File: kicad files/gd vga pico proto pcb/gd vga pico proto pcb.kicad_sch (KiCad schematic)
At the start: 0 parts

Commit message: floor planning complete
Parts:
- added C1: 10u, Capacitor_SMD:C_0805_2012Metric, symbol My Library:C_0805
- added C2, C3, C4: 1u, Capacitor_SMD:C_0805_2012Metric, symbol My Library:C_0805
- added J1: RGB Bin, Connector_PinSocket_2.54mm:PinSocket_2x04_P2.54mm_Vertical, symbol Connector_Generic:Conn_02x04_Odd_Even
- added J2: CLKS, Connector_PinSocket_2.54mm:PinSocket_2x04_P2.54mm_Vertical, symbol Connector_Generic:Conn_02x04_Odd_Even
- added J3: Conn_01x05, Connector_PinHeader_2.54mm:PinHeader_1x05_P2.54mm_Vertical, symbol Connector_Generic:Conn_01x05
- added J4: L77HDE15SD1CH4F, Connector_Dsub:DSUB-15-HD_Female_Horizontal_P2.29x1.98mm_EdgePinOffset8.35mm_Housed_MountingHolesOffset10.89mm, symbol Connector:DB15_Female_HighDensity_MountingHoles
- added J5: VID_TXRX, Connector_PinHeader_2.54mm:PinHeader_1x04_P2.54mm_Vertical, symbol Connector_Generic:Conn_01x04
- added J6: WIN, Connector_PinHeader_2.54mm:PinHeader_1x02_P2.54mm_Vertical, symbol Connector_Generic:Conn_01x02
- added J7: 5V, Connector_PinSocket_2.54mm:PinSocket_1x04_P2.54mm_Vertical, symbol Connector_Generic:Conn_01x04
- added JP1: 14M, Jumper:SolderJumper-2_P1.3mm_Bridged_RoundedPad1.0x1.5mm, symbol Jumper:SolderJumper_2_Bridged
- added JP2: 7M, Jumper:SolderJumper-2_P1.3mm_Open_TrianglePad1.0x1.5mm, symbol Jumper:SolderJumper_2_Open
- added R1, R10, R11: 100, Resistor_SMD:R_0603_1608Metric, symbol My_Library:R_0805
- added R2, R5, R8: 1k, Resistor_SMD:R_0603_1608Metric, symbol Device:R
- added R3: 390, Resistor_SMD:R_0603_1608Metric, symbol Device:R
- added R4, R7: 2k2, Resistor_SMD:R_0603_1608Metric, symbol Device:R
- added R6, R9: 470, Resistor_SMD:R_0603_1608Metric, symbol Device:R
- added RNP1, RNP2: 4k7, Resistor_SMD:R_0603_1608Metric, symbol My_Library:R_0805
- added SW1: RESET, My Libraries:SW_Push_CK_PTS525_SM15, symbol Switch:SW_Push
- added TP1, TP2, TP3, TP4, TP5, TP6, TP7, TP8: TestPoint_Harwin, My Libraries:Harwin-S1751-46-Test-Point, symbol My Library:TestPoint_Harwin
- added U1: Pico, RPi_Pico:RPi_Pico_SMD_TH, symbol RPi_Pico:Pico
- added U2: 74HCT245, Package_SO:SO-20_5.3x12.6mm_P1.27mm, symbol 74xx:74HC245
- added U3, U4: 74LVC2G04, Package_TO_SOT_SMD:SOT-23-6, symbol 74xGxx:74LVC2G04
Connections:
- new net: U3.3, U3.6
- new net: J4.13, R10.1
- new net: J4.14, R11.1
- new net: J4.9, R1.2
- new net: U4.3, U4.6
- new net +3.3V: U3.5 (+3.3V), U3.5 (+3.3V), U4.5 (+3.3V), U4.5 (+3.3V)
- new net +3V3: C2.1, C3.1, C4.1, J3.1 (Pin_1), RNP1.2, RNP2.2, U1.36 (3V3), U2.20 (VCC)
- new net +5V: C1.1, J7.1 (Pin_1), J7.2 (Pin_2), R1.1, U1.39 (VSYS), U2.1 (A->B)
- new net 14M: J2.1 (Pin_1), JP1.1 (A)
- new net 14M_J: JP1.2 (B), U2.9 (A7)
- new net 14M_RP: U1.22 (GPIO17), U2.12 (B6)
- new net 7M: J2.2 (Pin_2), JP2.1 (A)
- new net 7M_J: JP2.2 (B), U2.8 (A6)
- new net 7M_RP: U1.21 (GPIO16), U2.11 (B7)
- new net BLU0: R7.2, U1.7 (GPIO5)
- new net BLU1: R8.2, U1.9 (GPIO6)
- new net BLU2: R9.2, U1.10 (GPIO7)
- new net CREF: J2.3 (Pin_3)
- new net GND: C1.2, C2.2, C3.2, C4.2, J1.7 (Pin_7), J1.8 (Pin_8), J2.7 (Pin_7), J2.8 (Pin_8), J3.5 (Pin_5), J4.0, J4.10, J4.5, J4.6, J4.7, J4.8, J5.4 (Pin_4), J6.2 (Pin_2), J7.3 (Pin_3), J7.4 (Pin_4), SW1.2, TP4.1, TP5.1, U1.13 (GND), U1.18 (GND), U1.23 (GND), U1.28 (GND), U1.3 (GND), U1.33 (AGND), U1.38 (GND), U1.42 (GND), U1.8 (GND), U2.10 (GND), U2.19 (CE), U3.2 (GND), U3.2 (GND), U4.2 (GND), U4.2 (GND)
- new net GPIO10: U1.14 (GPIO10)
- new net GRN0: R4.2, U1.4 (GPIO2)
- new net GRN1: R5.2, U1.5 (GPIO3)
- new net GRN2: R6.2, U1.6 (GPIO4)
- new net HSYNC: R10.2, TP2.1, U1.11 (GPIO8)
- new net PH0: J2.5 (Pin_5)
- new net PICO_EN: TP1.1
- new net Q3: J2.4 (Pin_4)
- new net RED0: R2.2, U1.1 (GPIO0)
- new net RED1: R3.2, U1.2 (GPIO1)
- new net RGB1: J1.3 (Pin_3), U2.5 (A3)
- new net RGB1_RP: U1.24 (GPIO18), U2.15 (B3)
- new net RGB2: J1.5 (Pin_5), U2.4 (A2)
- new net RGB2_RP: U1.25 (GPIO19), U2.16 (B2)
- new net RGB4: J1.2 (Pin_2), U2.3 (A1)
- new net RGB4_RP: U1.26 (GPIO20), U2.17 (B1)
- new net RGB8: J1.4 (Pin_4), U2.2 (A0)
- new net RGB8_RP: U1.27 (GPIO21), U2.18 (B0)
- new net RUN: J3.4 (Pin_4), SW1.1, U1.30 (RUN)
- new net SERVIDEO: J1.6 (Pin_6), U3.1
- new net SERVID_RP: U1.29 (GPIO22), U3.4
- new net SWCLK: J3.3 (Pin_3), U1.41 (SWCLK)
- new net SWDIO: J3.2 (Pin_2), U1.43 (SWDIO)
- new net VBUS: U1.40 (VBUS)
- new net VGA_B: J4.3, R7.1, R8.1, R9.1, TP8.1
- new net VGA_G: J4.2, R4.1, R5.1, R6.1, TP7.1
- new net VGA_R: J4.1, R2.1, R3.1, TP6.1
- new net VGA_SCL: J4.15, RNP2.1, U1.32 (GPIO27_ADC1)
- new net VGA_SDA: J4.12, RNP1.1, U1.31 (GPIO26_ADC0)
- new net VID_RX: J5.3 (Pin_3), U1.17 (GPIO13)
- new net VID_TX: J5.2 (Pin_2), U1.16 (GPIO12)
- new net VIN_EN: J5.1 (Pin_1), U1.15 (GPIO11)
- new net VSYNC: R11.2, TP3.1, U1.12 (GPIO9)
- new net ~{RESET_RP}: U1.34 (GPIO28_ADC2), U4.4
- new net ~{RESET}: J2.6 (Pin_6), U4.1
- new net ~{SYNC_RP}: U1.19 (GPIO14), U2.14 (B4)
- new net ~{SYNC}: J1.1 (Pin_1), U2.6 (A4)
- new net ~{WINDOW_RP}: U1.20 (GPIO15), U2.13 (B5)
- new net ~{WINDOW}: J6.1 (Pin_1), U2.7 (A5)
- no-connect marks 0 -> 3
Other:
- note added: "Pico"
- note added: "VGA"
- note added: "VGA 'DAC'"

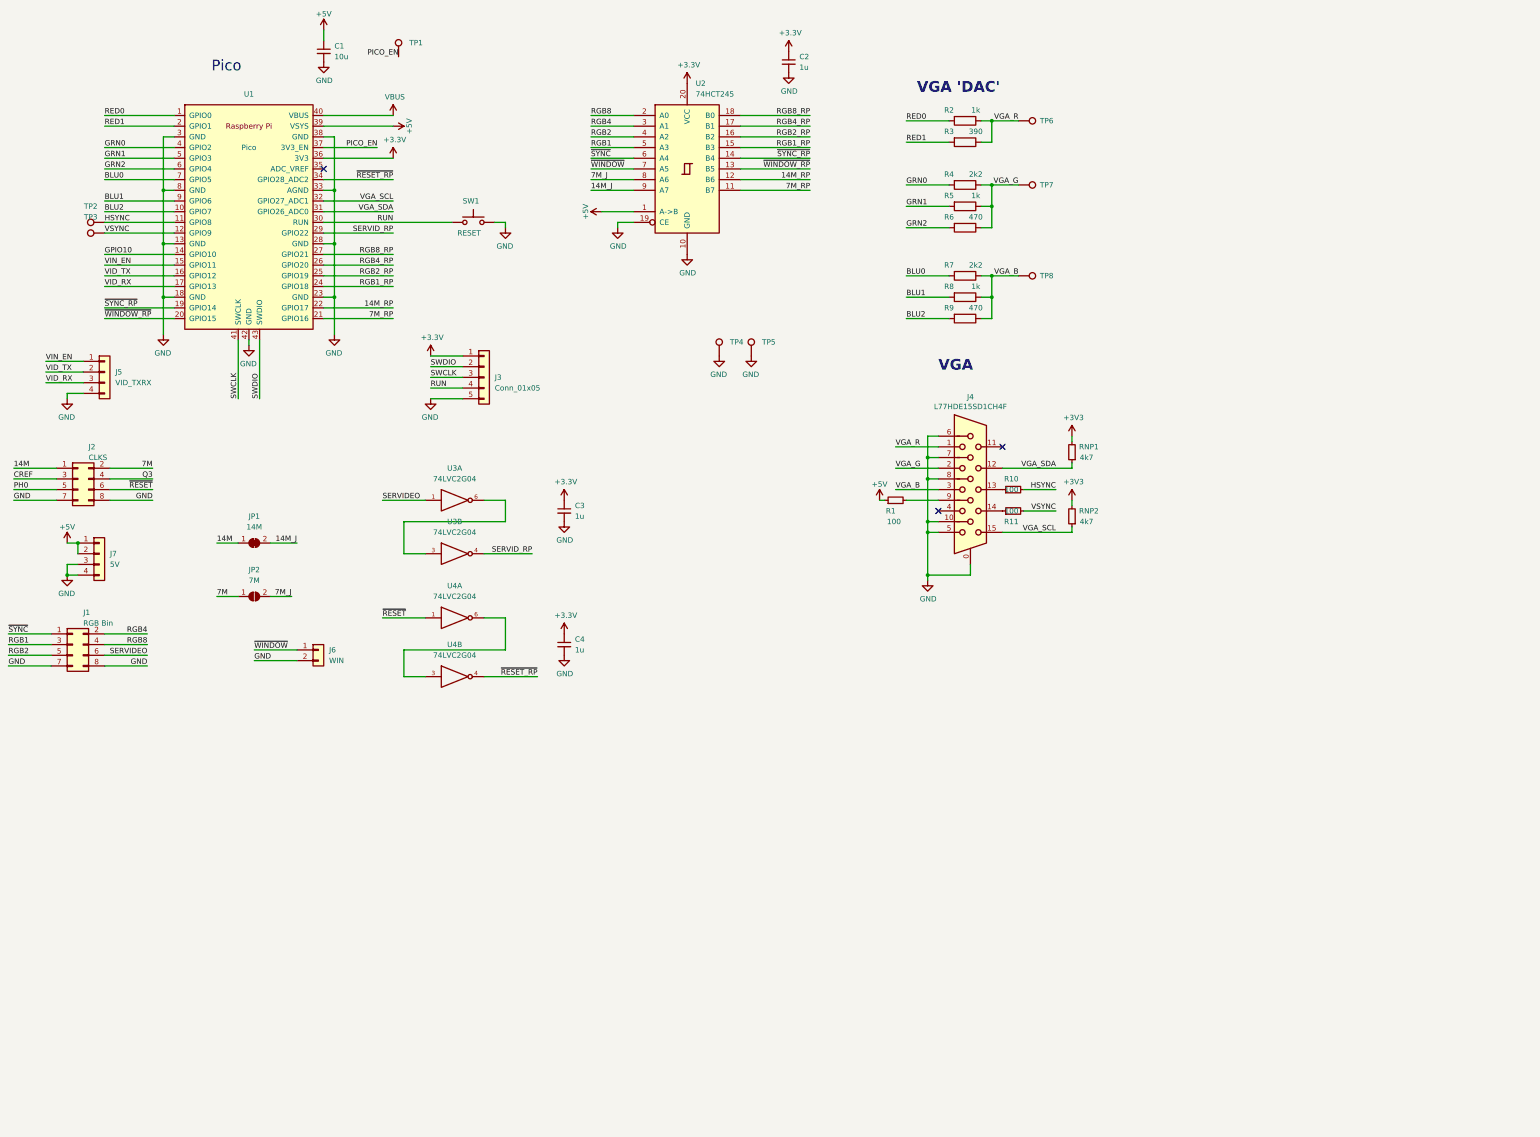
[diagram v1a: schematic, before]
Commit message: swapped from pico to RP2040--yay
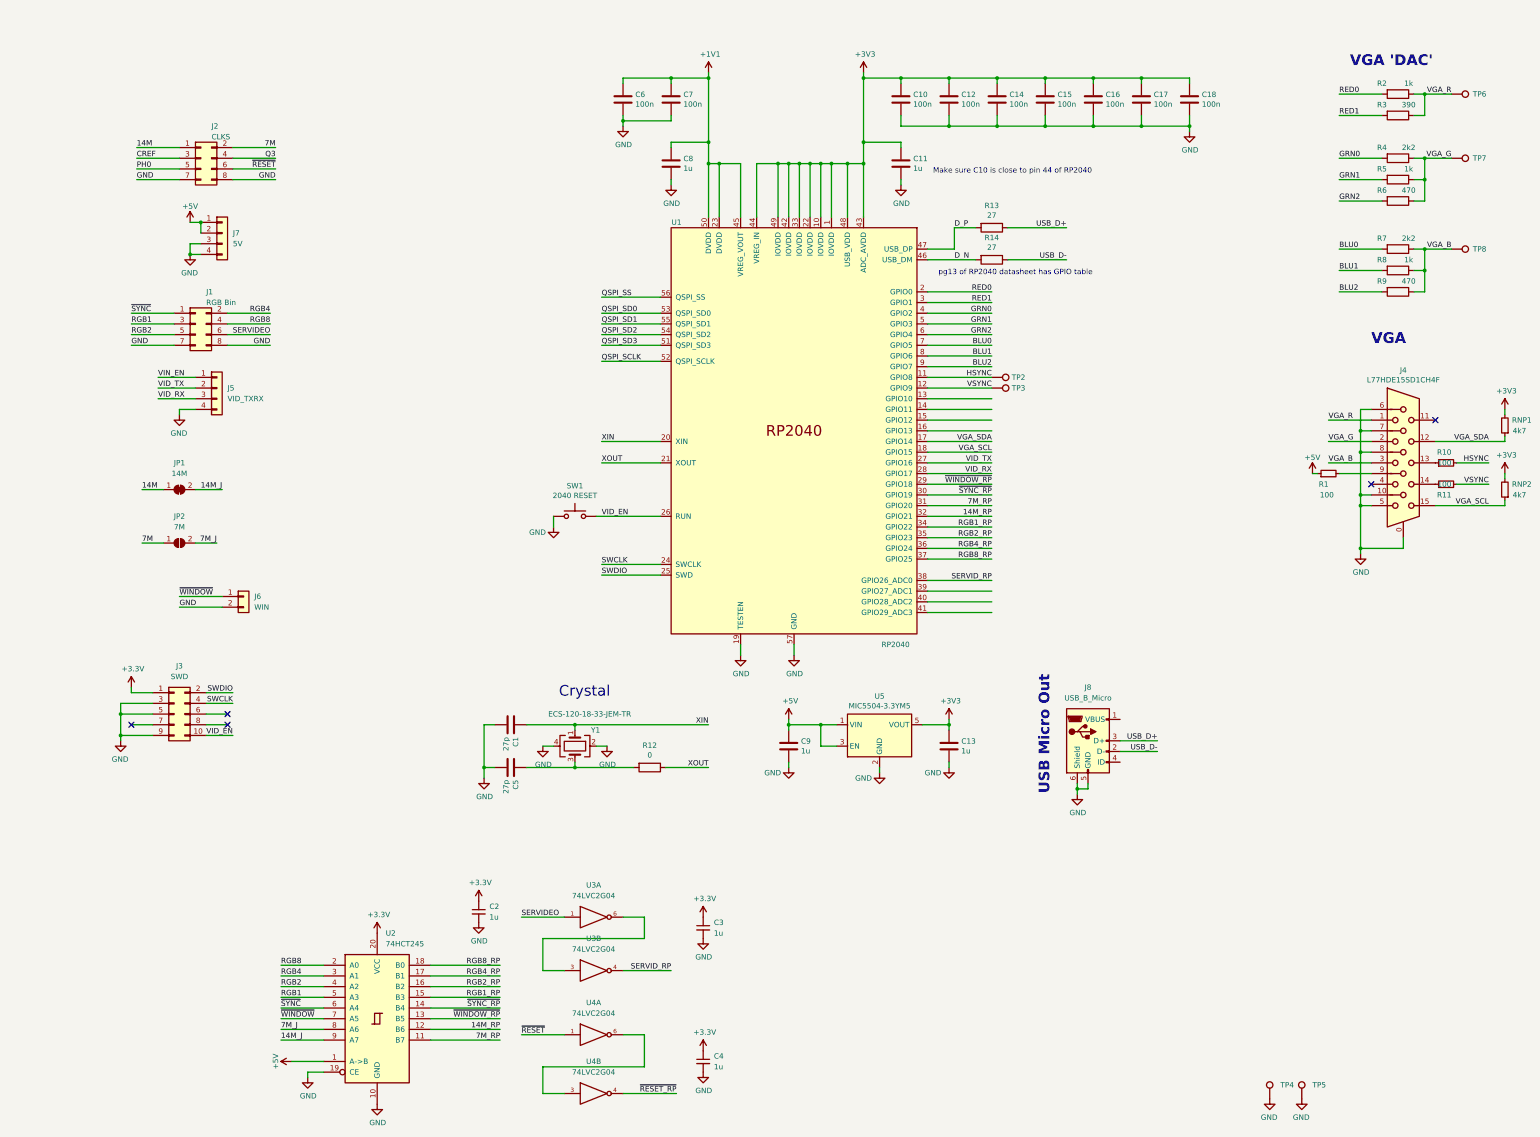
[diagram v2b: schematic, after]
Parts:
- removed C1: 10u, Capacitor_SMD:C_0805_2012Metric, symbol My Library:C_0805
- removed J3: Conn_01x05, Connector_PinHeader_2.54mm:PinHeader_1x05_P2.54mm_Vertical, symbol Connector_Generic:Conn_01x05
- removed TP1: TestPoint_Harwin, My Libraries:Harwin-S1751-46-Test-Point, symbol My Library:TestPoint_Harwin
- removed U1: Pico, RPi_Pico:RPi_Pico_SMD_TH, symbol RPi_Pico:Pico
- added C1, C5: 27p, Capacitor_SMD:C_0603_1608Metric, symbol Device:C
- added C10, C12, C14, C15, C16, C17, C18, C6, C7: 100n, Capacitor_SMD:C_0603_1608Metric, symbol Device:C
- added C11, C8: 1u, Capacitor_SMD:C_0603_1608Metric, symbol Device:C
- added C13, C9: 1u, Capacitor_SMD:C_0805_2012Metric, symbol Device:C
- added J3: SWD, Connector_PinSocket_1.27mm:PinSocket_2x05_P1.27mm_Vertical_SMD, symbol Connector_Generic:Conn_02x05_Odd_Even
- added J8: USB_B_Micro, Connector_USB:USB_Micro-B_GCT_USB3076-30-A, symbol Connector:USB_B_Micro
- added R12: 0, Resistor_SMD:R_0603_1608Metric, symbol Device:R
- added R13, R14: 27, Resistor_SMD:R_0603_1608Metric, symbol Device:R
- added U1: RP2040, RP2040_minimal:RP2040-QFN-56, symbol MCU_RaspberryPi_RP2040:RP2040
- added U5: MIC5504-3.3YM5, Package_TO_SOT_SMD:SOT-23-5, symbol Regulator_Linear:MIC5504-3.3YM5
- added Y1: ECS-120-18-33-JEM-TR, Crystal:Crystal_SMD_3225-4Pin_3.2x2.5mm, symbol Device:Crystal_GND24
- SW1: value RESET -> 2040 RESET
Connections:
- net RUN is gone; now on net GND: SW1.1
- net +3V3: now also C10.1, C11.1, C12.1, C13.1, C14.1, C15.1, C16.1, C17.1, C18.1, J3.1 (Pin_1), U1.1 (IOVDD), U1.10 (IOVDD), U1.22 (IOVDD), U1.33 (IOVDD), U1.42 (IOVDD), U1.43 (ADC_AVDD), U1.44 (VREG_IN), U1.48 (USB_VDD), U1.49 (IOVDD), U5.5 (VOUT)
- net +5V: now also C9.1, U5.1 (VIN), U5.3 (EN)
- net 14M_RP: now also U1.32 (GPIO21)
- net 7M_RP: now also U1.31 (GPIO20)
- net BLU0: now also U1.7 (GPIO5)
- net BLU1: now also U1.8 (GPIO6)
- net BLU2: now also U1.9 (GPIO7)
- net GND: now also C1.2, C10.2, C11.2, C12.2, C13.2, C14.2, C15.2, C16.2, C17.2, C18.2, C5.2, C6.2, C7.2, C8.2, C9.2, J3.3 (Pin_3), J3.5 (Pin_5), J3.9 (Pin_9), J8.5 (GND), J8.6 (Shield), U1.19 (TESTEN), U1.57 (GND), U5.2 (GND), Y1.2, Y1.4; no longer SW1.2
- net GRN0: now also U1.4 (GPIO2)
- net GRN1: now also U1.5 (GPIO3)
- net GRN2: now also U1.6 (GPIO4)
- net HSYNC: now also U1.11 (GPIO8)
- net RED0: now also U1.2 (GPIO0)
- net RED1: now also U1.3 (GPIO1)
- net RGB1_RP: now also U1.34 (GPIO22)
- net RGB2_RP: now also U1.35 (GPIO23)
- net RGB4_RP: now also U1.36 (GPIO24)
- net RGB8_RP: now also U1.37 (GPIO25)
- net SERVID_RP: now also U1.38 (GPIO26_ADC0)
- net SWCLK: now also J3.4 (Pin_4), U1.24 (SWCLK)
- net SWDIO: now also J3.2 (Pin_2), U1.25 (SWD)
- net VGA_SCL: now also U1.18 (GPIO15)
- net VGA_SDA: now also U1.17 (GPIO14)
- net VID_RX: now also U1.28 (GPIO17)
- net VID_TX: now also U1.27 (GPIO16)
- net VSYNC: now also U1.12 (GPIO9)
- net ~{SYNC_RP}: now also U1.30 (GPIO19)
- net ~{WINDOW_RP}: now also U1.29 (GPIO18)
- new net: C5.1, R12.2, Y1.3
- new net +1V1: C6.1, C7.1, C8.1, U1.23 (DVDD), U1.45 (VREG_VOUT), U1.50 (DVDD)
- new net D_N: R14.2, U1.46 (USB_DM)
- new net D_P: R13.2, U1.47 (USB_DP)
- new net QSPI_SCLK: U1.52 (QSPI_SCLK)
- new net QSPI_SD0: U1.53 (QSPI_SD0)
- new net QSPI_SD1: U1.55 (QSPI_SD1)
- new net QSPI_SD2: U1.54 (QSPI_SD2)
- new net QSPI_SD3: U1.51 (QSPI_SD3)
- new net QSPI_SS: U1.56 (QSPI_SS)
- new net USB_D+: J8.3 (D+), R13.1
- new net USB_D-: J8.2 (D-), R14.1
- new net VID_EN: J3.10 (Pin_10), SW1.2, U1.26 (RUN)
- new net XIN: C1.1, U1.20 (XIN), Y1.1
- new net XOUT: R12.1, U1.21 (XOUT)
- no-connect marks 3 -> 5
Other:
- note added: "Crystal"
- note added: "Make sure C10 is close to pin 44 of RP2040"
- note added: "USB Micro Out"
- note added: "pg13 of RP2040 datasheet has GPIO table"
- note removed: "Pico"
- moved on the sheet: C2, C3, C4, J1, J2, J4, J5, J6, J7, JP1, JP2, R1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
